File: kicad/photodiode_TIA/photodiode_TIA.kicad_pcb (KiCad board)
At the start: 2 copper layers, 25 x 10 mm, 8 parts, among them J3 Conn_01x03_Pin, U1 MCP6001R

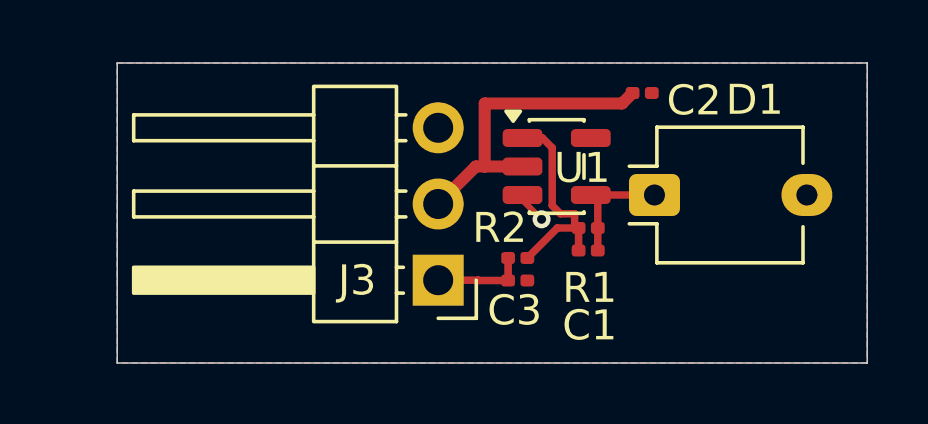
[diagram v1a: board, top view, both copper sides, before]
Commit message: added manufacturing files
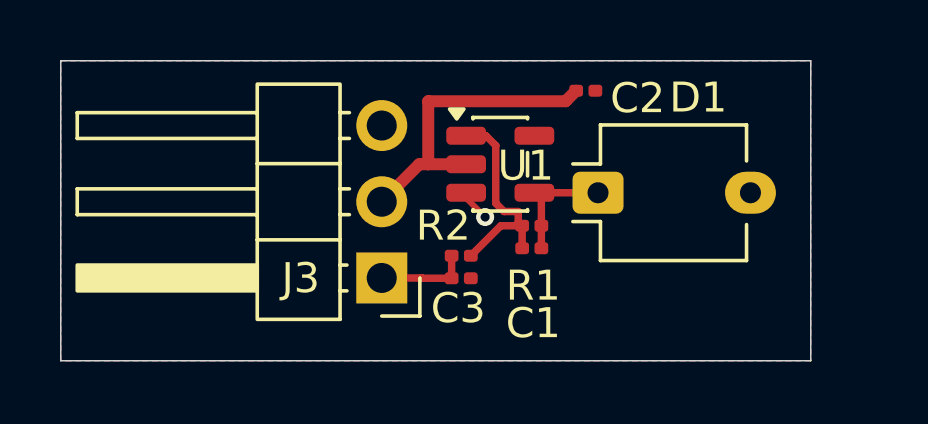
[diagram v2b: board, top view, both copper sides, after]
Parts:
- moved C3 1.88 mm to (178.2, 77.9)
- moved C1 1.88 mm to (180.6, 76.9)
- moved C2 1.88 mm to (182.4, 71.7)
- moved D1 1.88 mm to (182.8, 75.1)
- moved R1 1.88 mm to (180.6, 76.2)
- moved R2 1.88 mm to (178.2, 77.2)
- moved U1 1.88 mm to (179.5, 74.1)
- moved J3 1.88 mm to (175.6, 77.9)
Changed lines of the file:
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@@
 	(footprint "Connector_PinHeader_2.54mm:PinHeader_1x03_P2.54mm_Horizontal"
 		(layer "F.Cu")
-		(at 177.45 77.99 180)
+		(at 175.56875 77.915 180)
 		(descr "Through hole angled pin header, 1x03, 2.54mm pitch, 6mm pin length, single row")
 		(tags "Through hole angled pin header THT 1x03 2.54mm single row")
@@
 	(footprint "Capacitor_SMD:C_0201_0603Metric"
 		(layer "F.Cu")
-		(at 180.099554 78)
+		(at 178.218304 77.925)
 		(descr "Capacitor SMD 0201 (0603 Metric), square (rectangular) end terminal, IPC-7351 nominal, (Body size source: https://www.vishay.com/docs/20052/crcw0201e3.pdf), generated with kicad-footprint-generator")
 		(tags "capacitor")
@@
 	(footprint "Capacitor_SMD:C_0201_0603Metric"
 		(layer "F.Cu")
-		(at 182.45 77 180)
+		(at 180.56875 76.925 180)
 		(descr "Capacitor SMD 0201 (0603 Metric), square (rectangular) end terminal, IPC-7351 nominal, (Body size source: https://www.vishay.com/docs/20052/crcw0201e3.pdf), generated with kicad-footprint-generator")
 		(tags "capacitor")
@@
 	(footprint "Resistor_SMD:R_0201_0603Metric"
 		(layer "F.Cu")
-		(at 182.45 76.25 180)
+		(at 180.56875 76.175 180)
 		(descr "Resistor SMD 0201 (0603 Metric), square (rectangular) end terminal, IPC-7351 nominal, (Body size source: https://www.vishay.com/docs/20052/crcw0201e3.pdf), generated with kicad-footprint-generator")
 		(tags "resistor")
@@
 	(footprint "OptoDevice:Osram_DIL2_4.3x4.65mm_P5.08mm"
 		(layer "F.Cu")
-		(at 184.66 75.15)
+		(at 182.77875 75.075)
 		(descr "PhotoDiode, plastic DIL, 4.3x4.65mm², RM5.08")
 		(tags "PhotoDiode plastic DIL RM5.08")
@@
 	(footprint "Capacitor_SMD:C_0201_0603Metric"
 		(layer "F.Cu")
-		(at 184.25 71.75)
+		(at 182.36875 71.675)
 		(descr "Capacitor SMD 0201 (0603 Metric), square (rectangular) end terminal, IPC-7351 nominal, (Body size source: https://www.vishay.com/docs/20052/crcw0201e3.pdf), generated with kicad-footprint-generator")
 		(tags "capacitor")
@@
 	(footprint "Resistor_SMD:R_0201_0603Metric"
 		(layer "F.Cu")
-		(at 180.1 77.25 180)
+		(at 178.21875 77.175 180)
 		(descr "Resistor SMD 0201 (0603 Metric), square (rectangular) end terminal, IPC-7351 nominal, (Body size source: https://www.vishay.com/docs/20052/crcw0201e3.pdf), generated with kicad-footprint-generator")
 		(tags "resistor")
@@
 	(footprint "Package_TO_SOT_SMD:SOT-23-5"
 		(layer "F.Cu")
-		(at 181.4 74.2)
+		(at 179.51875 74.125)
 		(descr "SOT, 5 Pin (JEDEC MO-178 Var AA https://www.jedec.org/document_search?search_api_views_fulltext=MO-178), generated with kicad-footprint-generator ipc_gullwing_generator.py")
 		(tags "SOT TO_SOT_SMD")
@@
 	)
 	(gr_rect
-		(start 166.75 70.75)
-		(end 191.75 80.75)
+		(start 164.86875 70.675)
+		(end 189.86875 80.675)
 		(stroke
 			(width 0.05)
@@
 	)
 	(segment
-		(start 182 75.776)
-		(end 181.526 75.776)
+		(start 180.11875 75.701)
+		(end 179.64475 75.701)
 		(width 0.25)
 		(layer "F.Cu")
@@
 	)
 	(segment
-		(start 182 76.12)
-		(end 182 75.776)
+		(start 180.11875 76.045)
+		(end 180.11875 75.701)
 		(width 0.25)
 		(layer "F.Cu")
@@
 	)
 	(segment
-		(start 180.42 77.25)
-		(end 181.42 76.25)
+		(start 178.53875 77.175)
+		(end 179.53875 76.175)
 		(width 0.25)
 		(layer "F.Cu")
@@
 	)
 	(segment
-		(start 181.251 73.576001)
-		(end 180.924999 73.25)
+		(start 179.36975 73.501001)
+		(end 179.043749 73.175)
 		(width 0.25)
 		(layer "F.Cu")
@@
 	)
 	(segment
-		(start 182.13 77)
-		(end 182.13 76.25)
+		(start 180.24875 76.925)
+		(end 180.24875 76.175)
 		(width 0.25)
 		(layer "F.Cu")
@@
 	)
 	(segment
-		(start 181.251 75.501)
-		(end 181.251 73.576001)
+		(start 179.36975 75.426)
+		(end 179.36975 73.501001)
 		(width 0.25)
 		(layer "F.Cu")
@@
 	)
 	(segment
-		(start 181.42 76.25)
-		(end 182.13 76.25)
+		(start 179.53875 76.175)
+		(end 180.24875 76.175)
 		(width 0.25)
 		(layer "F.Cu")
@@
 	)
 	(segment
-		(start 180.924999 73.25)
-		(end 180.2625 73.25)
+		(start 179.043749 73.175)
+		(end 178.38125 73.175)
 		(width 0.25)
 		(layer "F.Cu")
@@
 	)
 	(segment
-		(start 181.526 75.776)
-		(end 181.251 75.501)
+		(start 179.64475 75.701)
+		(end 179.36975 75.426)
 		(width 0.25)
 		(layer "F.Cu")
@@
 	)
 	(segment
-		(start 182.13 76.25)
-		(end 182 76.12)
+		(start 180.24875 76.175)
+		(end 180.11875 76.045)
 		(width 0.25)
 		(layer "F.Cu")
@@
 	)
 	(segment
-		(start 182.77 75.3825)
-		(end 182.5375 75.15)
+		(start 180.88875 75.3075)
+		(end 180.65625 75.075)
 		(width 0.2)
 		(layer "F.Cu")
@@
 	)
 	(segment
-		(start 182.5375 75.15)
-		(end 184.66 75.15)
+		(start 180.65625 75.075)
+		(end 182.77875 75.075)
 		(width 0.25)
 		(layer "F.Cu")
@@
 	)
 	(segment
-		(start 182.77 77)
-		(end 182.77 75.3825)
+		(start 180.88875 76.925)
+		(end 180.88875 75.3075)
 		(width 0.25)
 		(layer "F.Cu")
@@
 	)
 	(segment
-		(start 179 72.1)
-		(end 183.58 72.1)
+		(start 177.11875 72.025)
+		(end 181.69875 72.025)
 		(width 0.4)
 		(layer "F.Cu")
@@
 	)
 	(segment
-		(start 179 74.2)
-		(end 180.2625 74.2)
+		(start 177.11875 74.125)
+		(end 178.38125 74.125)
 		(width 0.4)
 		(layer "F.Cu")
@@
 	)
 	(segment
-		(start 177.45 75.45)
-		(end 178.7 74.2)
+		(start 175.56875 75.375)
+		(end 176.81875 74.125)
 		(width 0.4)
 		(layer "F.Cu")
@@
 	)
 	(segment
-		(start 178.7 74.2)
-		(end 179 74.2)
+		(start 176.81875 74.125)
+		(end 177.11875 74.125)
 		(width 0.4)
 		(layer "F.Cu")
@@
 	)
 	(segment
-		(start 179 74.2)
-		(end 179 72.1)
+		(start 177.11875 74.125)
+		(end 177.11875 72.025)
 		(width 0.4)
 		(layer "F.Cu")
@@
 	)
 	(segment
-		(start 183.58 72.1)
-		(end 183.93 71.75)
+		(start 181.69875 72.025)
+		(end 182.04875 71.675)
 		(width 0.4)
 		(layer "F.Cu")
@@
 	)
 	(segment
-		(start 180.2625 75.15)
-		(end 180.2625 75.325674)
+		(start 178.38125 75.075)
+		(end 178.38125 75.250674)
 		(width 0.2)
 		(layer "F.Cu")
@@
 	)
 	(segment
-		(start 180.2625 75.325674)
-		(end 180.896827 75.960001)
+		(start 178.38125 75.250674)
+		(end 179.015577 75.885001)
 		(width 0.2)
 		(layer "F.Cu")
@@
 	)
 	(via
-		(at 180.896827 75.960001)
+		(at 179.015577 75.885001)
 		(size 0.6)
 		(drill 0.3)
@@
 	)
 	(segment
-		(start 178.782966 77.99)
-		(end 177.45 77.99)
+		(start 176.901716 77.915)
+		(end 175.56875 77.915)
 		(width 0.25)
 		(layer "F.Cu")
@@
 	)
 	(segment
-		(start 179.78 77.999554)
-		(end 179.779554 78)
+		(start 177.89875 77.924554)
+		(end 177.898304 77.925)
 		(width 0.2)
 		(layer "F.Cu")
@@
 	)
 	(segment
-		(start 179.779554 78)
-		(end 178.792966 78)
+		(start 177.898304 77.925)
+		(end 176.911716 77.925)
 		(width 0.25)
 		(layer "F.Cu")
@@
 	)
 	(segment
-		(start 178.792966 78)
-		(end 178.782966 77.99)
+		(start 176.911716 77.925)
+		(end 176.901716 77.915)
 		(width 0.25)
 		(layer "F.Cu")
@@
 	)
 	(segment
-		(start 179.78 77.25)
-		(end 179.78 77.999554)
+		(start 177.89875 77.175)
+		(end 177.89875 77.924554)
 		(width 0.25)
 		(layer "F.Cu")
@@
 		(polygon
 			(pts
-				(xy 191.75 70.75) (xy 191.75 80.75) (xy 166.75 80.75) (xy 166.75 70.75)
-			)
-		)
+				(xy 189.86875 70.675) (xy 189.86875 80.675) (xy 164.86875 80.675) (xy 164.86875 70.675)
+			)
+		)
